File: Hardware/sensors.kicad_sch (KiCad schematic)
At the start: 6 parts, among them U4 DPS310XTSA1

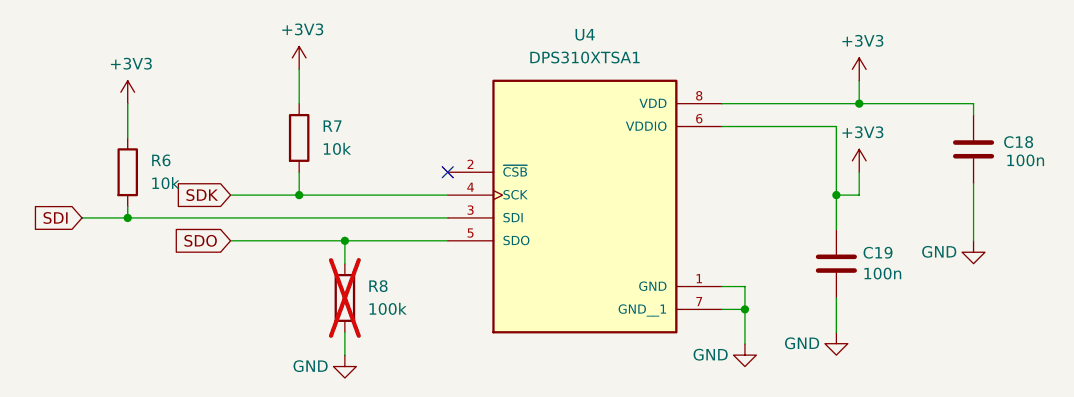
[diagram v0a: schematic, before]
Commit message: Added new components to sch and pcb and redid the routing and layout of pcb
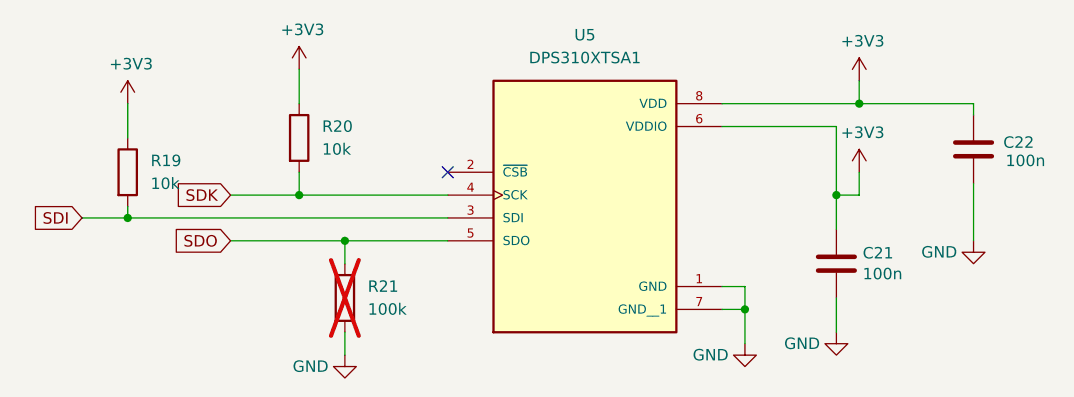
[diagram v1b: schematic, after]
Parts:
- R19: renamed from R6; footprint Resistor_SMD:R_0603_1608Metric -> Resistor_SMD:R_0402_1005Metric
- R20: renamed from R7; footprint Resistor_SMD:R_0603_1608Metric -> Resistor_SMD:R_0402_1005Metric
- R21: renamed from R8; footprint Resistor_SMD:R_0603_1608Metric -> Resistor_SMD:R_0402_1005Metric
- renumbered C19 to C21, C18 to C22, U4 to U5
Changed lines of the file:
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@@
 		(dnp no)
 		(fields_autoplaced yes)
-		(property "Reference" "R6"
+		(property "Reference" "R19"
 			(at 33.02 46.9899 0)
 			(effects
@@
 			)
 		)
-		(property "Footprint" "Resistor_SMD:R_0603_1608Metric"
+		(property "Footprint" "Resistor_SMD:R_0402_1005Metric"
 			(at 28.702 48.26 90)
 			(effects
@@
 			(project "chute_release"
 				(path "/9d05c756-443f-4d4d-9854-905483bdebb5/5f724fc2-c244-4ef5-a561-90477baa6d29"
-					(reference "R6")
+					(reference "R19")
 					(unit 1)
 				)
@@
 		(on_board yes)
 		(dnp no)
-		(property "Reference" "#PWR031"
+		(property "Reference" "#PWR052"
 			(at 109.22 72.39 0)
 			(effects
@@
 			(project "chute_release"
 				(path "/9d05c756-443f-4d4d-9854-905483bdebb5/5f724fc2-c244-4ef5-a561-90477baa6d29"
-					(reference "#PWR031")
+					(reference "#PWR052")
 					(unit 1)
 				)
@@
 		(on_board yes)
 		(dnp no)
-		(property "Reference" "C19"
+		(property "Reference" "C21"
 			(at 112.141 57.2516 0)
 			(effects
@@
 			(project "chute_release"
 				(path "/9d05c756-443f-4d4d-9854-905483bdebb5/5f724fc2-c244-4ef5-a561-90477baa6d29"
-					(reference "C19")
+					(reference "C21")
 					(unit 1)
 				)
@@
 		(on_board yes)
 		(dnp no)
-		(property "Reference" "C18"
+		(property "Reference" "C22"
 			(at 127.762 44.958 0)
 			(effects
@@
 			(project "chute_release"
 				(path "/9d05c756-443f-4d4d-9854-905483bdebb5/5f724fc2-c244-4ef5-a561-90477baa6d29"
-					(reference "C18")
+					(reference "C22")
 					(unit 1)
 				)
@@
 		(dnp yes)
 		(fields_autoplaced yes)
-		(property "Reference" "R8"
+		(property "Reference" "R21"
 			(at 57.15 60.9599 0)
 			(effects
@@
 			)
 		)
-		(property "Footprint" "Resistor_SMD:R_0603_1608Metric"
+		(property "Footprint" "Resistor_SMD:R_0402_1005Metric"
 			(at 52.832 62.23 90)
 			(effects
@@
 			(project "chute_release"
 				(path "/9d05c756-443f-4d4d-9854-905483bdebb5/5f724fc2-c244-4ef5-a561-90477baa6d29"
-					(reference "R8")
+					(reference "R21")
 					(unit 1)
 				)
@@
 		(on_board yes)
 		(dnp no)
-		(property "Reference" "#PWR029"
+		(property "Reference" "#PWR054"
 			(at 111.76 52.07 0)
 			(effects
@@
 			(project "chute_release"
 				(path "/9d05c756-443f-4d4d-9854-905483bdebb5/5f724fc2-c244-4ef5-a561-90477baa6d29"
-					(reference "#PWR029")
+					(reference "#PWR054")
 					(unit 1)
 				)
@@
 		(dnp no)
 		(fields_autoplaced yes)
-		(property "Reference" "R7"
+		(property "Reference" "R20"
 			(at 52.07 43.1799 0)
 			(effects
@@
 			)
 		)
-		(property "Footprint" "Resistor_SMD:R_0603_1608Metric"
+		(property "Footprint" "Resistor_SMD:R_0402_1005Metric"
 			(at 47.752 44.45 90)
 			(effects
@@
 			(project "chute_release"
 				(path "/9d05c756-443f-4d4d-9854-905483bdebb5/5f724fc2-c244-4ef5-a561-90477baa6d29"
-					(reference "R7")
+					(reference "R20")
 					(unit 1)
 				)
@@
 		(dnp no)
 		(fields_autoplaced yes)
-		(property "Reference" "U4"
+		(property "Reference" "U5"
 			(at 81.28 33.02 0)
 			(effects
@@
 			(project ""
 				(path "/9d05c756-443f-4d4d-9854-905483bdebb5/5f724fc2-c244-4ef5-a561-90477baa6d29"
-					(reference "U4")
+					(reference "U5")
 					(unit 1)
 				)
@@
 		(on_board yes)
 		(dnp no)
-		(property "Reference" "#PWR032"
+		(property "Reference" "#PWR050"
 			(at 54.61 74.93 0)
 			(effects
@@
 			(project "chute_release"
 				(path "/9d05c756-443f-4d4d-9854-905483bdebb5/5f724fc2-c244-4ef5-a561-90477baa6d29"
-					(reference "#PWR032")
+					(reference "#PWR050")
 					(unit 1)
 				)
@@
 		(on_board yes)
 		(dnp no)
-		(property "Reference" "#PWR030"
+		(property "Reference" "#PWR055"
 			(at 124.46 62.23 0)
 			(effects
@@
 			(project "chute_release"
 				(path "/9d05c756-443f-4d4d-9854-905483bdebb5/5f724fc2-c244-4ef5-a561-90477baa6d29"
-					(reference "#PWR030")
+					(reference "#PWR055")
 					(unit 1)
 				)
@@
 		(on_board yes)
 		(dnp no)
-		(property "Reference" "#PWR026"
+		(property "Reference" "#PWR051"
 			(at 99.06 73.66 0)
 			(effects
@@
 			(project "chute_release"
 				(path "/9d05c756-443f-4d4d-9854-905483bdebb5/5f724fc2-c244-4ef5-a561-90477baa6d29"
-					(reference "#PWR026")
+					(reference "#PWR051")
 					(unit 1)
 				)
@@
 		(on_board yes)
 		(dnp no)
-		(property "Reference" "#PWR028"
+		(property "Reference" "#PWR049"
 			(at 49.53 40.64 0)
 			(effects
@@
 			(project "chute_release"
 				(path "/9d05c756-443f-4d4d-9854-905483bdebb5/5f724fc2-c244-4ef5-a561-90477baa6d29"
-					(reference "#PWR028")
+					(reference "#PWR049")
 					(unit 1)
 				)
@@
 		(on_board yes)
 		(dnp no)
-		(property "Reference" "#PWR027"
+		(property "Reference" "#PWR048"
 			(at 30.48 44.45 0)
 			(effects
@@
 			(project "chute_release"
 				(path "/9d05c756-443f-4d4d-9854-905483bdebb5/5f724fc2-c244-4ef5-a561-90477baa6d29"
-					(reference "#PWR027")
+					(reference "#PWR048")
 					(unit 1)
 				)
@@
 		(on_board yes)
 		(dnp no)
-		(property "Reference" "#PWR025"
+		(property "Reference" "#PWR053"
 			(at 111.76 41.91 0)
 			(effects
@@
 			(project "chute_release"
 				(path "/9d05c756-443f-4d4d-9854-905483bdebb5/5f724fc2-c244-4ef5-a561-90477baa6d29"
-					(reference "#PWR025")
-					(unit 1)
-				)
+					(reference "#PWR053")
+					(unit 1)
+				)

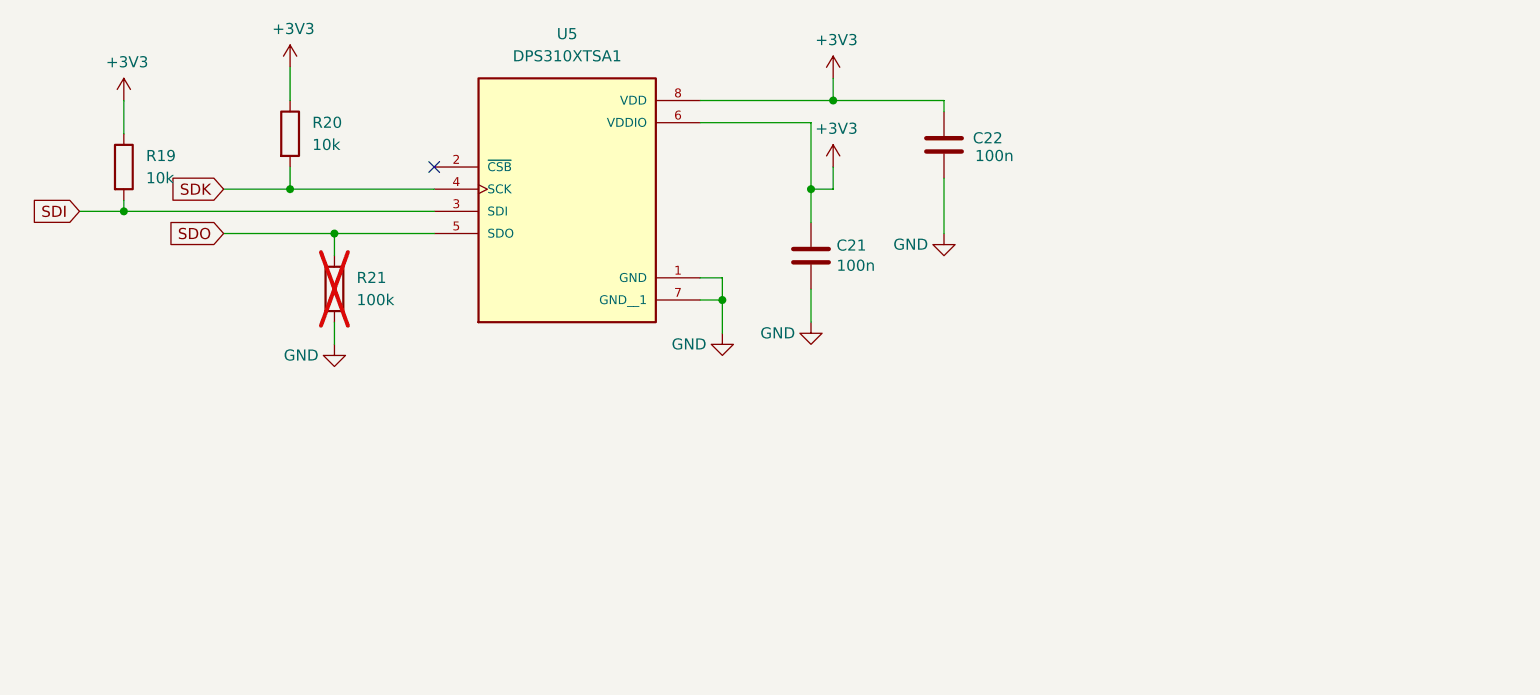
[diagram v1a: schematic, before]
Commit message: Added external batt switch pin and bypass 0ohm res, changed ldo for smaller 600mA
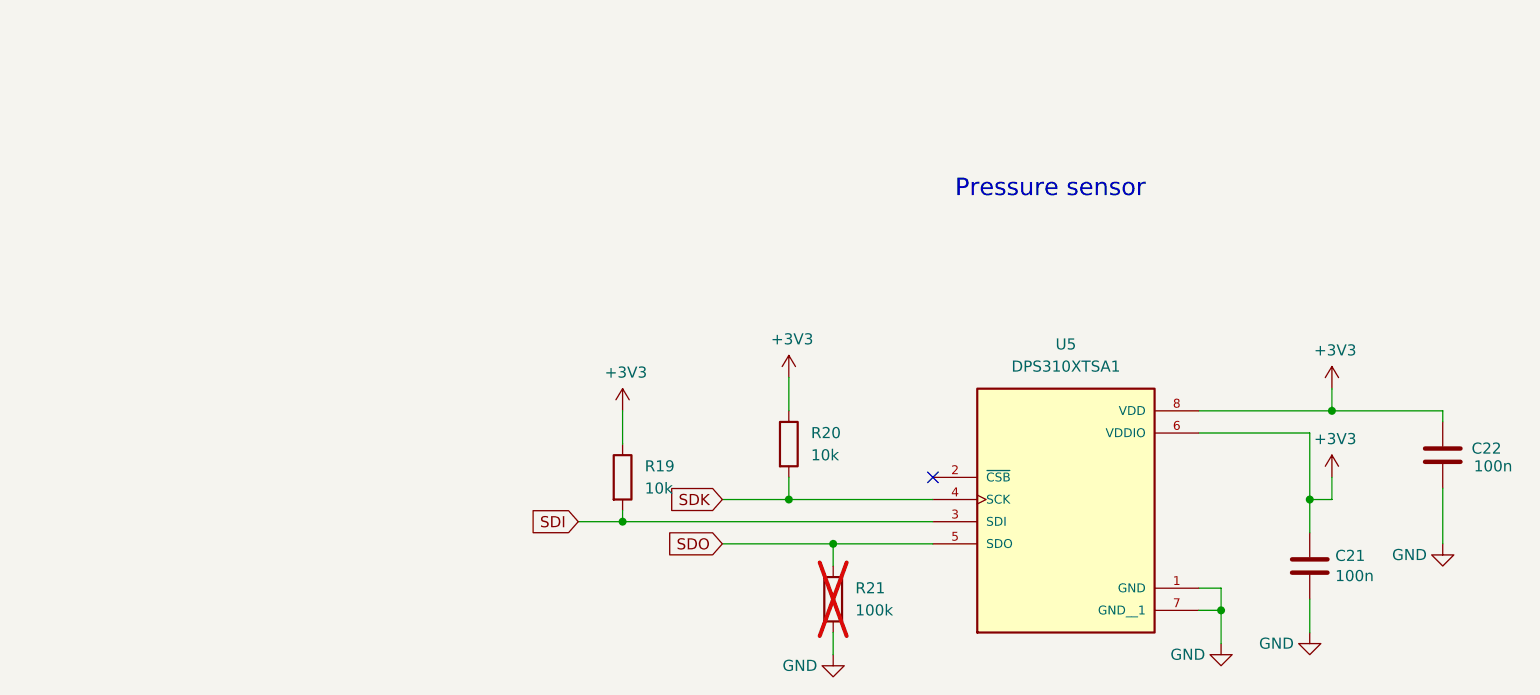
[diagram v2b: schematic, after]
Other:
- note added: "Pressure sensor"
- moved on the sheet: C21, C22, R19, R20, R21, U5
